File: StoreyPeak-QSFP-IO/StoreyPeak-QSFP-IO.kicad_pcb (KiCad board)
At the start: 2 copper layers, 30.1 x 69.8 mm, 21 parts, among them J1 USB_B_Micro, J2 HDMI_A_1.4, U1 QSFP_PCB-QSFP, U2 FT232RL

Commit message: Changes
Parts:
- removed D1: RX, LED_SMD:LED_0805_2012Metric_Pad1.15x1.40mm_HandSolder
- removed D2: TX, LED_SMD:LED_0805_2012Metric_Pad1.15x1.40mm_HandSolder
- removed J2: HDMI_A_1.4, CarlosEDP_Lib:CONN-10029449-111RLF
- removed R7, R8: 47, Resistor_SMD:R_0603_1608Metric_Pad0.98x0.95mm_HandSolder
- added HDMI1: HD-A-05H9191N, easyeda2kicad:HDMI-SMD_HD-A-05H9192N, B.Cu at (167.2, 127.5)
- C1, C2, F1, R1, R2, U2: moved to B.Cu
- moved R2 18.5 mm to (156.4, 96.6), turned to 180 degrees
- moved F1 13.6 mm to (154.1, 125.5), turned to -90 degrees
- moved R1 13.5 mm to (159.9, 96.7), turned to 180 degrees
- moved U2 8.62 mm to (159.2, 88.2)
- moved C1 8.15 mm to (159.9, 93.6), turned to 180 degrees
- moved C2 7.93 mm to (159.9, 95.2), turned to 180 degrees
- moved C3 7.05 mm to (167.7, 118.7)
- moved C4 7.05 mm to (166.2, 118.7)
- moved C5 7.05 mm to (164.6, 118.7)
- moved C10 7.05 mm to (169.3, 118.7)
- moved C6 7.05 mm to (163.0, 118.7)
- moved C7 7.05 mm to (161.4, 118.7)
- moved C8 7.05 mm to (159.9, 118.7)
- moved C9 7.05 mm to (170.9, 118.7)
- moved J1 0.45 mm to (152.4, 129.9)
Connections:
- net Net-(J1-Pad2) renamed /USB_D-
- net Net-(J1-Pad3) renamed /USB_D+
- U2 pad 22: Net-(D1-Pad2) -> unconnected-(U2-CBUS1-Pad22)
- U2 pad 23: Net-(D2-Pad2) -> unconnected-(U2-CBUS0-Pad23)
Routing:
- net Net-(D2-Pad2): track 69.0 -> 0.00 mm, vias 2 -> 0
- net Net-(D1-Pad2): track 39.2 -> 0.00 mm
- net +5V: track 82.9 -> 58.0 mm, vias 1 -> 0
- net Net-(J1-VBUS): track 20.2 -> 2.12 mm, vias 1 -> 0
- net /QSFP_D2-: track 48.4 -> 63.4 mm
- net /QSFP_D2+: track 48.1 -> 62.8 mm
- net /QSFP_D0+: track 52.6 -> 66.4 mm
- net Net-(D1-Pad1): track 13.4 -> 0.00 mm
- net /QSFP_D0-: track 55.6 -> 67.2 mm
- net /USB_D+: track 53.5 -> 42.0 mm, vias 1 -> 2
- net Net-(U1-SCL): track 13.9 -> 22.9 mm, vias 1 -> 2
- net /HDMI_D2-: track 13.9 -> 5.49 mm
- net /HDMI_D1+: track 13.7 -> 5.55 mm
- net /HDMI_D1-: track 13.2 -> 5.16 mm
- net /HDMI_CLK-: track 13.6 -> 5.63 mm
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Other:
- outline, holes or cut-outs redrawn
- board text removed: "@CarlosEDP - 2021 https://github.com/carlosedp"
- board text removed: "BOTTOM"
- board text removed: "TOP"

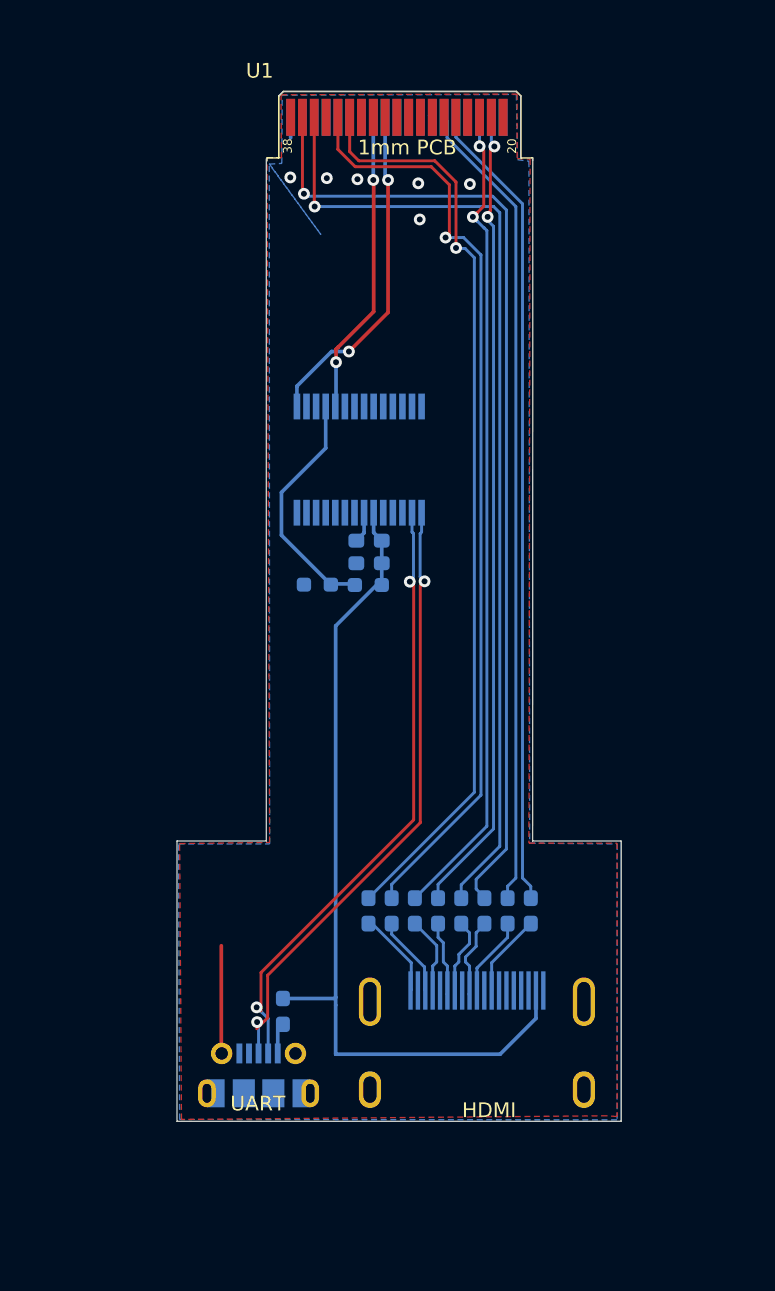
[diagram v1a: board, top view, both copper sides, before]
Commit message: Use CH340G UART and USB-C port
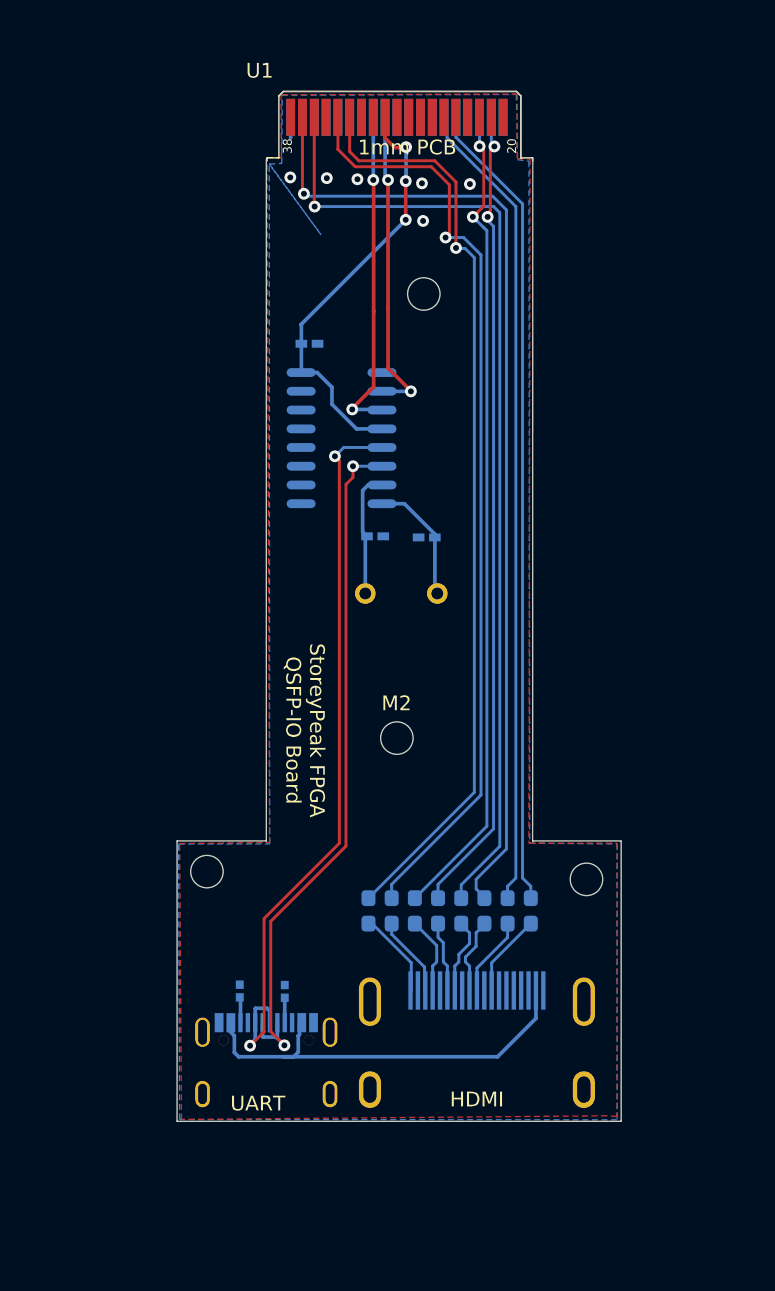
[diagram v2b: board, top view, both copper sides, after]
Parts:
- removed F1: Polyfuse_Small, Fuse:Fuse_0603_1608Metric_Pad1.05x0.95mm_HandSolder
- removed J1: USB_B_Micro, CarlosEDP_Lib:USB_Micro-B_Molex-105017-0001
- added ?: , , F.Cu at (163.6, 76.9)
- added ?: , , F.Cu at (174.7, 116.6)
- added ?: , , F.Cu at (148.9, 116.1)
- added C11: TCC0402X7R102M500AT, easyeda2kicad:C0402, B.Cu at (155.9, 80.3)
- added M2: MountingHole_2.2mm_M2, MountingHole:MountingHole_2.2mm_M2, F.Cu at (161.8, 107.0)
- added U3: CH340G, easyeda2kicad:SOIC-16_L9.9-W3.9-P1.27-LS6.0-BL, B.Cu at (158.1, 86.7)
- added USB1: KH-TYPE-C-16P-T, easyeda2kicad:USB-C-SMD_KH-TYPE-C-16P, B.Cu at (152.9, 128.7)
- C1: value 0.1u -> TCC0402COG200J500AT; footprint Capacitor_SMD:C_0603_1608Metric_Pad1.08x0.95mm_HandSolder -> easyeda2kicad:C0402
- C2: value 10u -> TCC0402COG200J500AT; footprint Capacitor_SMD:C_0603_1608Metric_Pad1.08x0.95mm_HandSolder -> easyeda2kicad:C0402
- R1, R2: value 4k7 -> 0402WGJ0512TCE; footprint Resistor_SMD:R_0603_1608Metric_Pad0.98x0.95mm_HandSolder -> easyeda2kicad:R0402
- U2: value FT232RL -> WTL49S1220; footprint Package_SO:SSOP-28_5.3x10.2mm_P0.65mm -> easyeda2kicad:CRYSTAL-TH_L11.1-W4.7
- moved R1 28.1 mm to (154.2, 124.2), turned to -90 degrees
- moved R2 28.0 mm to (151.2, 124.2), turned to -90 degrees
- moved U2 9.51 mm to (162.1, 97.2), turned to 0 degrees
- moved C2 4.29 mm to (163.8, 93.4), turned to 0 degrees
- moved C1 0.51 mm to (160.3, 93.3)
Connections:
- C1 pad 1: +5V -> GND
- C1 pad 2: GND -> Net-(U2-OSC1)
- C2 pad 1: +5V -> GND
- C2 pad 2: GND -> Net-(U2-OSC2)
- R1 pad 1: +5V -> GND
- R1 pad 2: +2V5 -> Net-(USB1-CC1)
- R2 pad 1: +2V5 -> GND
- R2 pad 2: GND -> Net-(USB1-CC2)
- U1 pad 30: unconnected-(U1-Vcc1-Pad30) -> +3V3
- U2 pad 1: Net-(U1-SCL) -> Net-(U2-OSC1)
- U2 pad 2: unconnected-(U2-DTR-Pad2) -> Net-(U2-OSC2)
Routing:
- net +3V3: track 0.00 -> 29.9 mm, vias 0 -> 3
- net +5V: track 58.0 -> 28.6 mm
- net +2V5: track 16.0 -> 0.00 mm
- net GND: track 11.5 -> 1.67 mm
- net /USB_D+: track 42.0 -> 50.9 mm
- net Net-(U2-OSC1): track 0.00 -> 8.62 mm
- net Net-(U2-OSC2): track 0.00 -> 8.53 mm
- net /USB_D-: track 41.8 -> 47.7 mm
- net Net-(J1-VBUS): track 2.12 -> 0.00 mm
- net Net-(U1-SDA): track 20.6 -> 22.5 mm
- net Net-(USB1-CC2): track 0.00 -> 1.73 mm
- net Net-(USB1-CC1): track 0.00 -> 1.72 mm
- net Net-(U1-SCL): track 22.9 -> 21.4 mm

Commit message: Use passives from JLCPCB basic library
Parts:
- C1, C2: value TCC0402COG200J500AT -> 0402CG200J500NT
- C11: value TCC0402X7R102M500AT -> 0402B102K500NT
- R1, R2: value 0402WGJ0512TCE -> 0402WGF5101TCE
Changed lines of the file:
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@@
 			)
 		)
-		(property "Value" "TCC0402COG200J500AT"
+		(property "Value" "0402CG200J500NT"
 			(at 0 -4 360)
 			(layer "B.Fab")
@@
 			)
 		)
-		(property "Datasheet" ""
+		(property "Datasheet" "https://lcsc.com/product-detail/Multilayer-Ceramic-Capacitors-MLCC-SMD-SMT_20pF-200-5-50V_C1554.html"
 			(at 0 0 180)
 			(unlocked yes)
@@
 			)
 		)
-		(property "LCSC Part" "C880615"
+		(property "LCSC Part" "C1554"
 			(at 0 0 180)
 			(unlocked yes)
@@
 			(net 1 "GND")
 			(pinfunction "1")
-			(pintype "unspecified")
+			(pintype "input")
 		)
 		(pad "2" smd rect
@@
 			(net 43 "Net-(U2-OSC2)")
 			(pinfunction "2")
-			(pintype "unspecified")
+			(pintype "input")
 		)
 		(model "${EASYEDA2KICAD}/easyeda2kicad.3dshapes/C0402_L1.0-W0.5-H0.5.wrl"
@@
 			)
 		)
-		(property "Value" "0402WGJ0512TCE"
+		(property "Value" "0402WGF5101TCE"
 			(at 0 -4 90)
 			(layer "B.Fab")
@@
 			)
 		)
-		(property "Datasheet" "https://lcsc.com/product-detail/Chip-Resistor-Surface-Mount-UniOhm_5-1KR-512-5_C25941.html"
+		(property "Datasheet" "https://lcsc.com/product-detail/Chip-Resistor-Surface-Mount-UniOhm_5-1KR-5101-1_C25905.html"
 			(at 0 0 90)
 			(unlocked yes)
@@
 			)
 		)
-		(property "LCSC Part" "C25941"
+		(property "LCSC Part" "C25905"
 			(at 0 0 90)
 			(unlocked yes)
@@
 			)
 		)
-		(property "Value" "TCC0402COG200J500AT"
+		(property "Value" "0402CG200J500NT"
 			(at 0 -4 180)
 			(layer "B.Fab")
@@
 			)
 		)
-		(property "Datasheet" ""
+		(property "Datasheet" "https://lcsc.com/product-detail/Multilayer-Ceramic-Capacitors-MLCC-SMD-SMT_20pF-200-5-50V_C1554.html"
 			(at 0 0 0)
 			(unlocked yes)
@@
 			)
 		)
-		(property "LCSC Part" "C880615"
+		(property "LCSC Part" "C1554"
 			(at 0 0 0)
 			(unlocked yes)
@@
 			(net 1 "GND")
 			(pinfunction "1")
-			(pintype "unspecified")
+			(pintype "input")
 		)
 		(pad "2" smd rect
@@
 			(net 35 "Net-(U2-OSC1)")
 			(pinfunction "2")
-			(pintype "unspecified")
+			(pintype "input")
 		)
 		(model "${EASYEDA2KICAD}/easyeda2kicad.3dshapes/C0402_L1.0-W0.5-H0.5.wrl"
@@
 			)
 		)
-		(property "Value" "TCC0402X7R102M500AT"
+		(property "Value" "0402B102K500NT"
 			(at 0 -4 180)
 			(layer "B.Fab")
@@
 			)
 		)
-		(property "Datasheet" "https://lcsc.com/product-detail/Multilayer-Ceramic-Capacitors-MLCC-SMD-SMT_CCTC-TCC0402X7R102M500AT_C696907.html"
+		(property "Datasheet" "https://lcsc.com/product-detail/Multilayer-Ceramic-Capacitors-MLCC-SMD-SMT_1nF-102-10-50V_C1523.html"
 			(at 0 0 0)
 			(unlocked yes)
@@
 			)
 		)
-		(property "LCSC Part" "C696907"
+		(property "LCSC Part" "C1523"
 			(at 0 0 0)
 			(unlocked yes)
@@
 			(net 1 "GND")
 			(pinfunction "1")
-			(pintype "unspecified")
+			(pintype "input")
 		)
 		(pad "2" smd rect
@@
 			(net 44 "+3V3")
 			(pinfunction "2")
-			(pintype "unspecified")
+			(pintype "input")
 		)
 		(model "${EASYEDA2KICAD}/easyeda2kicad.3dshapes/C0402_L1.0-W0.5-H0.5.wrl"
@@
 			)
 		)
-		(property "Value" "0402WGJ0512TCE"
+		(property "Value" "0402WGF5101TCE"
 			(at 0 -4 90)
 			(layer "B.Fab")
@@
 			)
 		)
-		(property "Datasheet" "https://lcsc.com/product-detail/Chip-Resistor-Surface-Mount-UniOhm_5-1KR-512-5_C25941.html"
+		(property "Datasheet" "https://lcsc.com/product-detail/Chip-Resistor-Surface-Mount-UniOhm_5-1KR-5101-1_C25905.html"
 			(at 0 0 90)
 			(unlocked yes)
@@
 			)
 		)
-		(property "LCSC Part" "C25941"
+		(property "LCSC Part" "C25905"
 			(at 0 0 90)
 			(unlocked yes)

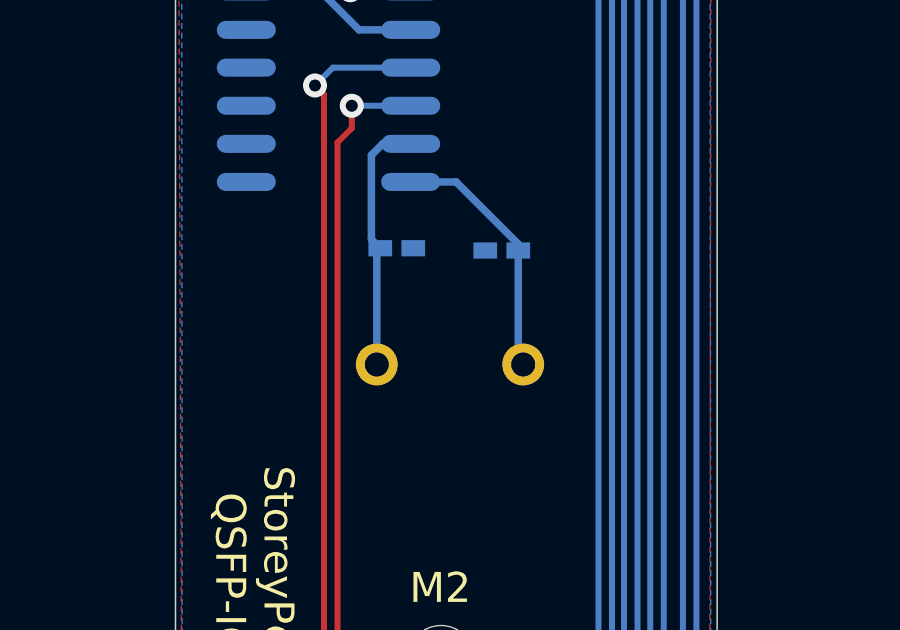
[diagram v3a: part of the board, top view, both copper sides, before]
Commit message: Use SMD crystal instead of THT
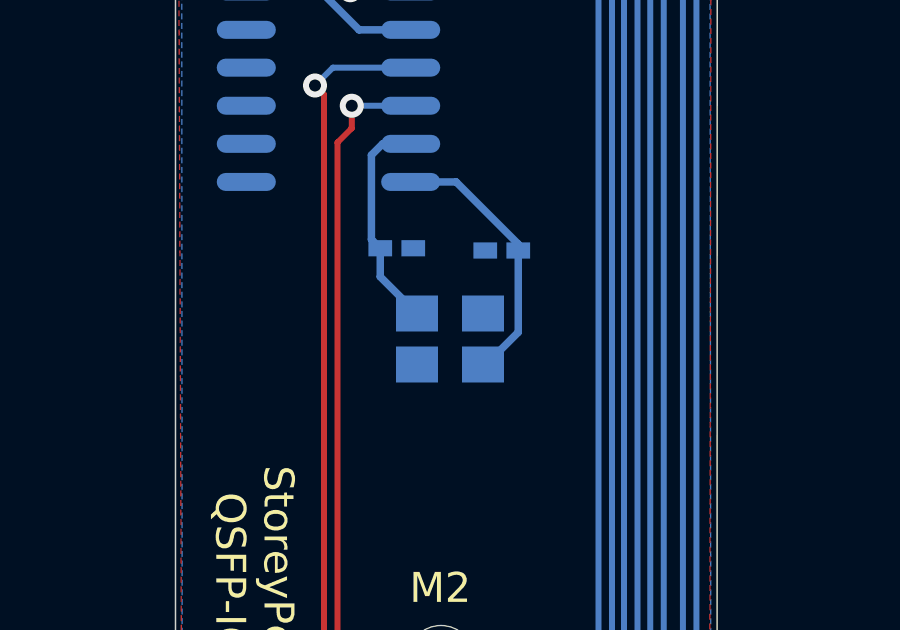
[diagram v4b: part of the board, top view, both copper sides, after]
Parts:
- removed U2: WTL49S1220, easyeda2kicad:CRYSTAL-TH_L11.1-W4.7
- added X1: X322512MSB4SI, easyeda2kicad:CRYSTAL-SMD_4P-L3.2-W2.5-BL, B.Cu at (162.1, 96.4)
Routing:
- net Net-(U3-XI): track 8.62 -> 7.54 mm

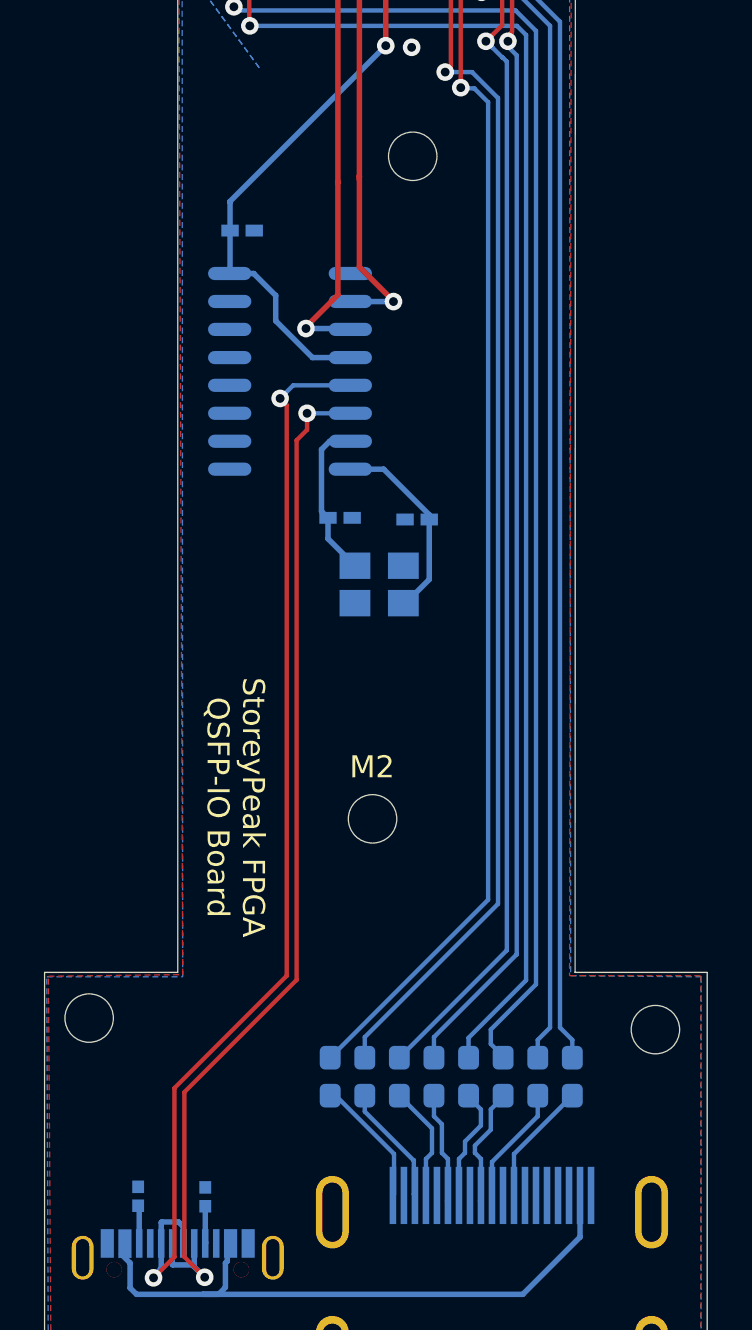
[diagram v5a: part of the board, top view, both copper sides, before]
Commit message: Add test points, add screw holes to schematic
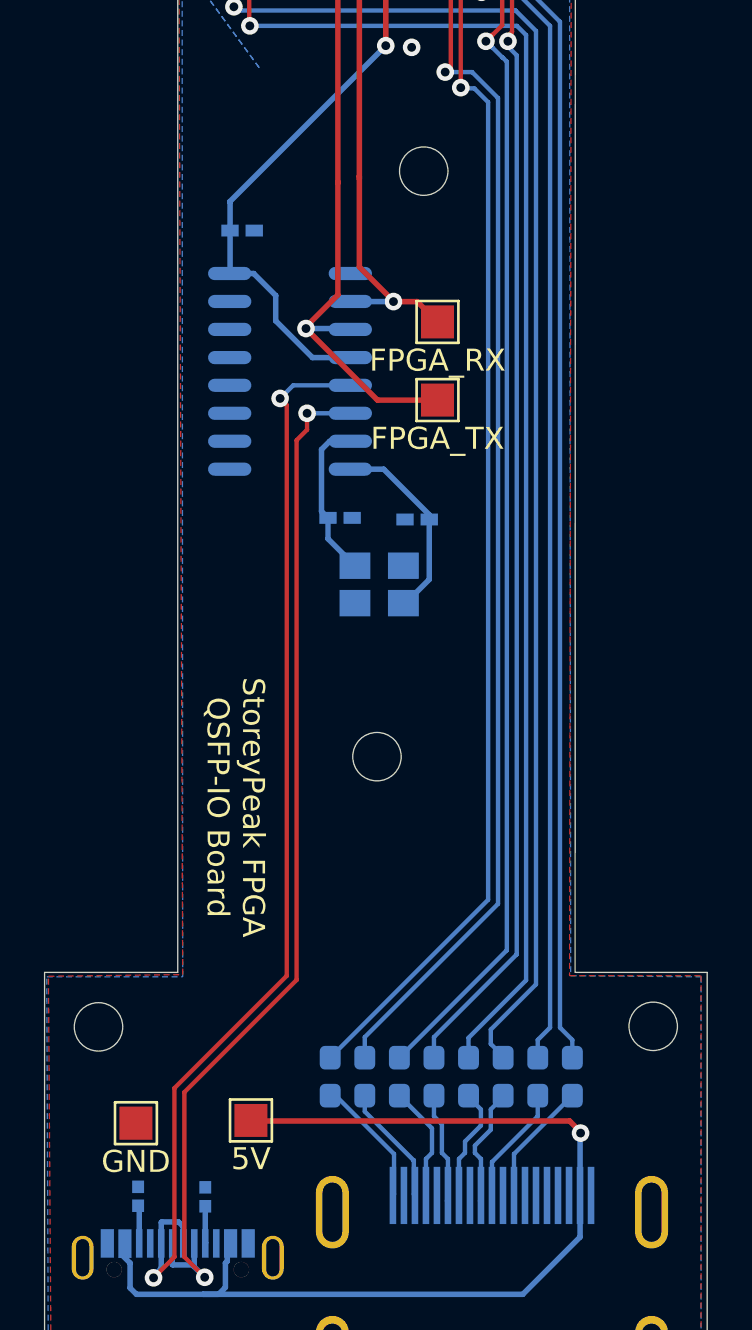
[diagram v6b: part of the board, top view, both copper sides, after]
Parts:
- removed ? (x3): , 
- removed M2: MountingHole_2.2mm_M2, MountingHole:MountingHole_2.2mm_M2
- added H1: MountingHole, MountingHole:MountingHole_2.2mm_M2, F.Cu at (164.1, 77.6)
- added H2: MountingHole, MountingHole:MountingHole_2.2mm_M2, F.Cu at (162.0, 104.2)
- added H3: MountingHole, MountingHole:MountingHole_2.2mm_M2, F.Cu at (174.6, 116.5)
- added H4: MountingHole, MountingHole:MountingHole_2.2mm_M2, F.Cu at (149.3, 116.5)
- added TP1: 5V, TestPoint:TestPoint_Pad_1.5x1.5mm, F.Cu at (156.3, 120.7)
- added TP2: GND, TestPoint:TestPoint_Pad_1.5x1.5mm, F.Cu at (151.1, 120.8)
- added TP3: FPGA_RX, TestPoint:TestPoint_Pad_1.5x1.5mm, F.Cu at (164.8, 84.5)
- added TP4: FPGA_TX, TestPoint:TestPoint_Pad_1.5x1.5mm, F.Cu at (164.8, 88.0)
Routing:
- net +5V: track 28.6 -> 46.9 mm, vias 0 -> 1
- net Net-(U1-SDA): track 22.5 -> 29.8 mm
- net Net-(U1-SCL): track 21.4 -> 23.8 mm
